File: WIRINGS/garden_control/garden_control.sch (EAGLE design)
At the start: 12 parts

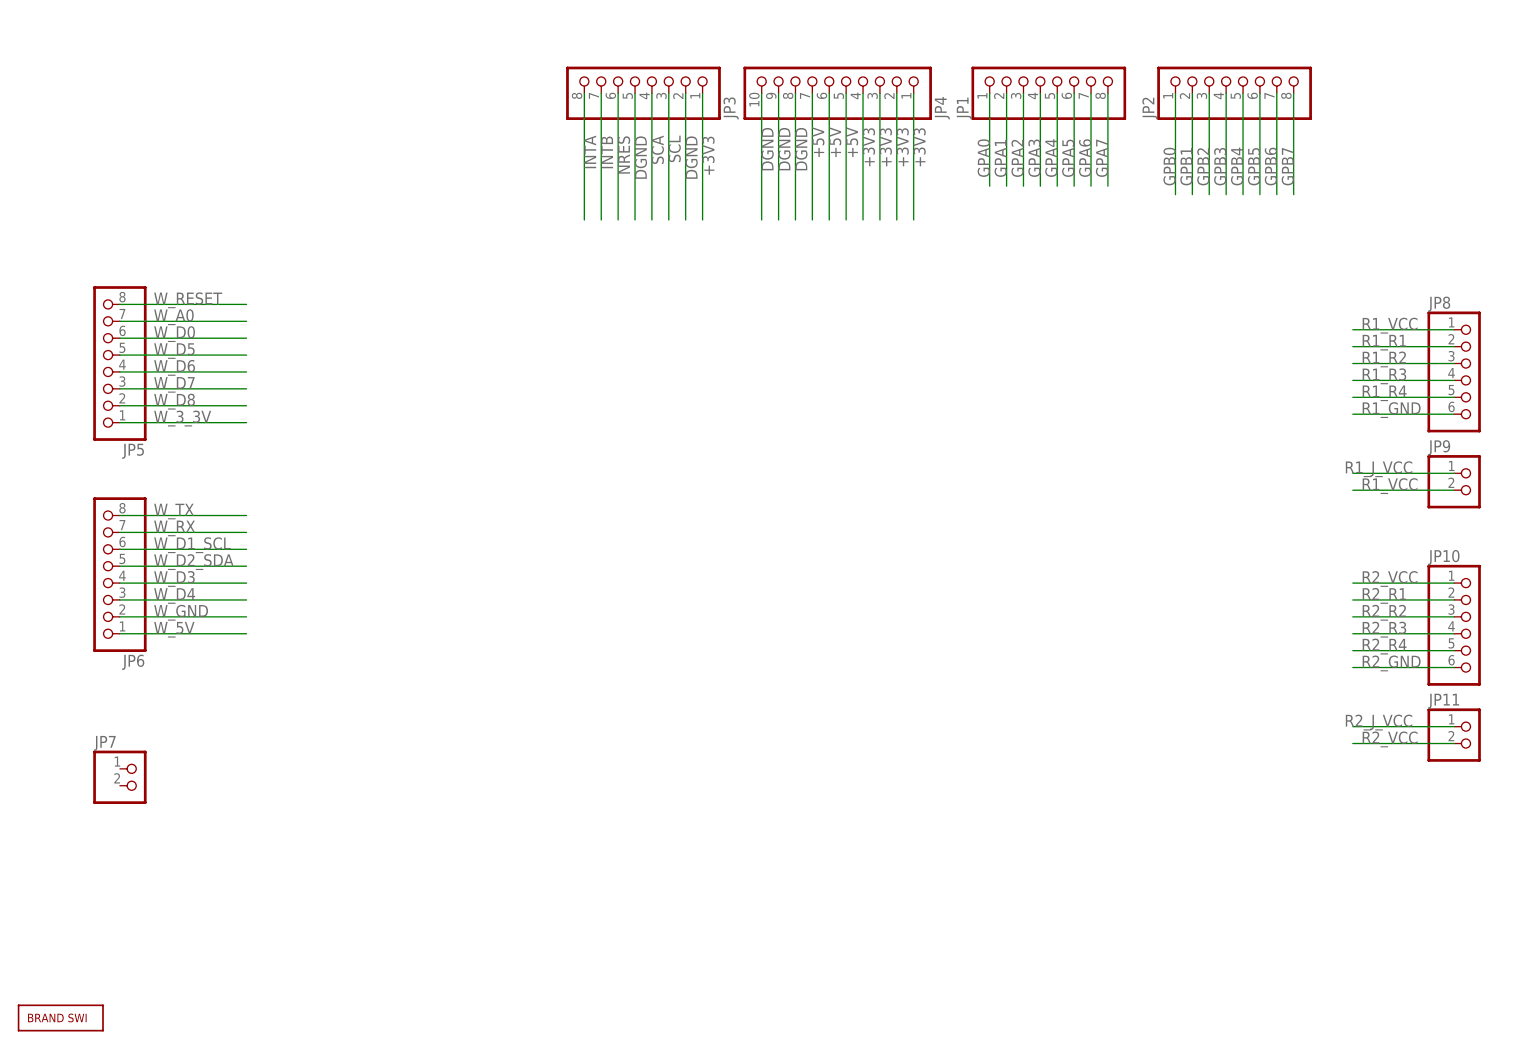
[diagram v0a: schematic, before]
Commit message: updated wiring
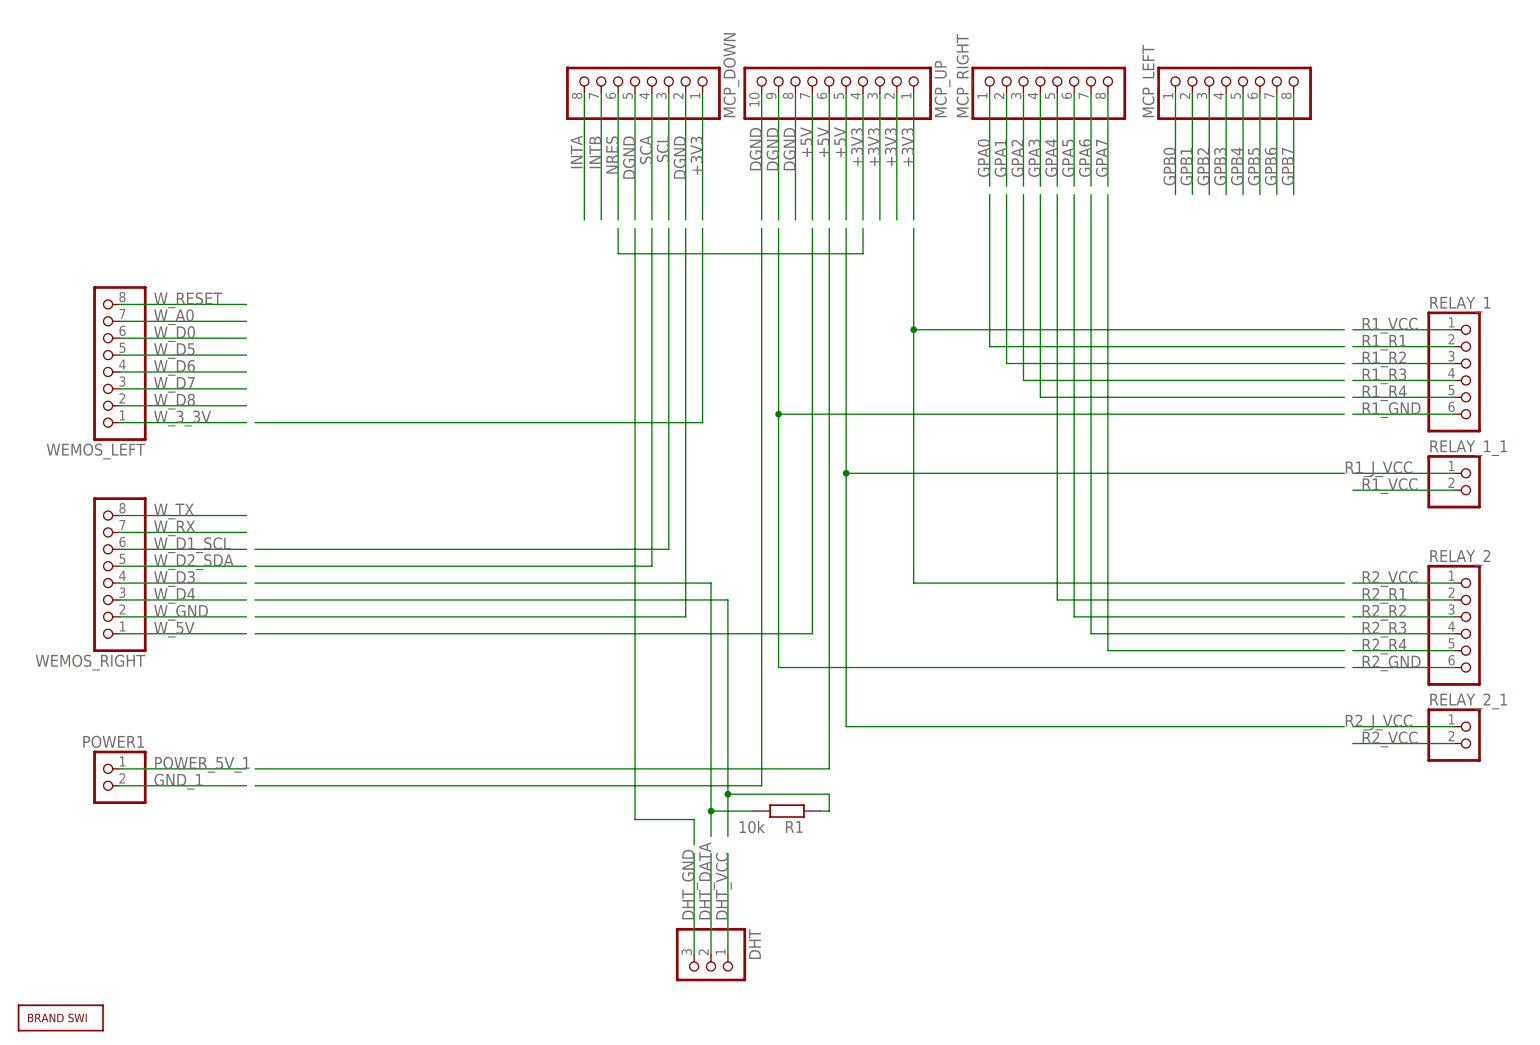
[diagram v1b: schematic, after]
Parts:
- removed JP7: (no value), pinhead:PINHD-1X2
- added DHT: (no value), pinhead:PINHD-1X3
- added POWER1: (no value), pinhead:PINHD-1X2
- added R1: 10k, rcl:R-EU_0207/10
- renumbered JP1 to MCP_RIGHT, JP10 to RELAY_2, JP11 to RELAY_2_1, JP2 to MCP_LEFT, JP3 to MCP_DOWN, JP4 to MCP_UP, JP5 to WEMOS_LEFT, JP6 to WEMOS_RIGHT, JP8 to RELAY_1, JP9 to RELAY_1_1
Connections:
- new net DHT_DATA: DHT.2
- new net DHT_GND: DHT.3
- new net DHT_VCC: DHT.1
- new net GND_1: POWER1.2
- new net N$4: R1.2
- new net N$5: R1.1
- new net POWER_5V_1: POWER1.1
